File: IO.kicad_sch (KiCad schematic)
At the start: 19 parts, among them J502 I2C, J503 SPI, J601 JST_SHBM04B-SRSS-TB, SW601 B3U-3000P, SW602 B3U-3000P, U601 SHTC3, U602 74LVC1G07SE-7, U603 74LVC1G07SE-7

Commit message: power symbols
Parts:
- removed U603: 74LVC1G07SE-7, Package_TO_SOT_SMD:SOT-353_SC-70-5, symbol CM4IO:74LVC1G07_copy
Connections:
- net nLED_ACTIVITY: now reaches R606.2
- net 3V3 renamed +3V3_PI
- net +3V3_PI: now also D606.2 (A)
- net 5V renamed +5V
- net +5V: no longer D606.2 (A)

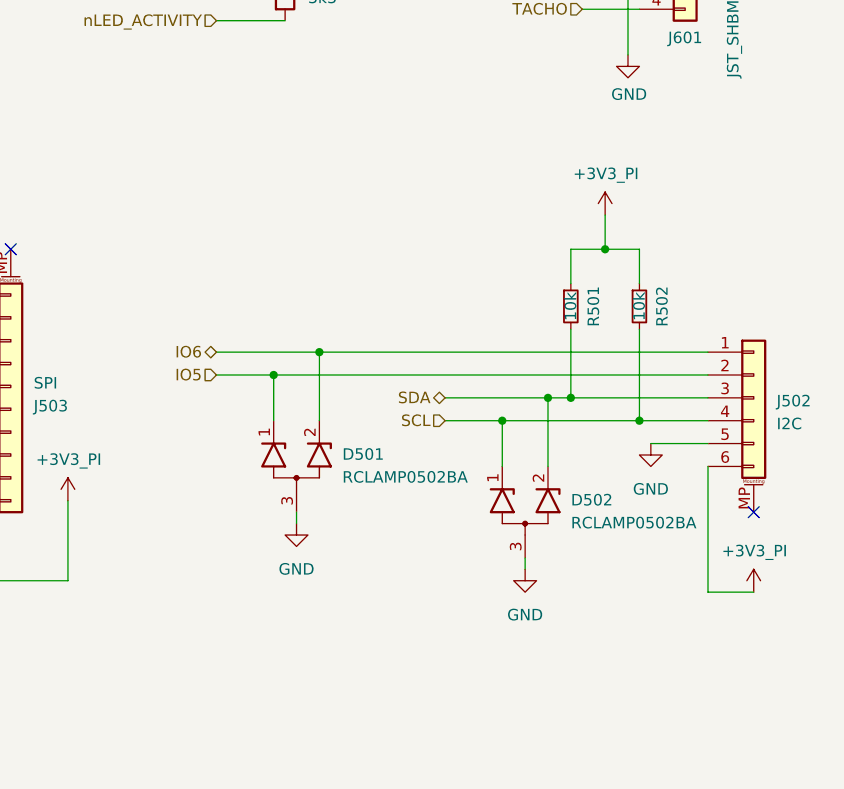
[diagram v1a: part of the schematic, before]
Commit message: changed i2c connector and nrpiboot
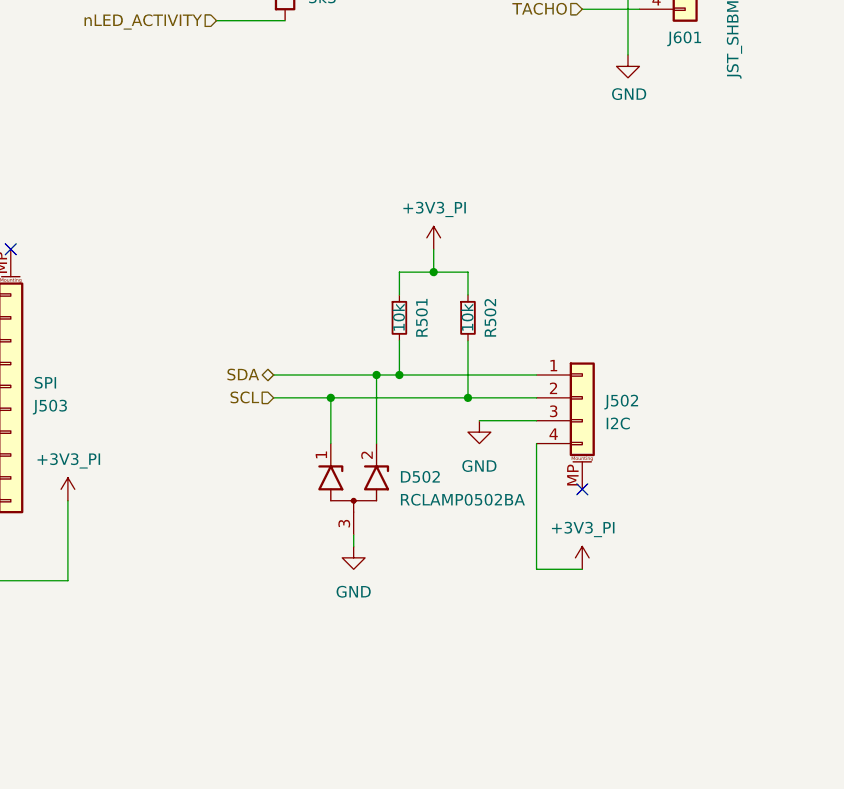
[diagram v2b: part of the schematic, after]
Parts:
- removed D501: RCLAMP0502BA, Package_TO_SOT_SMD:SOT-416, symbol Power_Protection:RCLAMP0502BA
- J502: footprint Connector_JST:JST_SH_BM06B-SRSS-TB_1x06-1MP_P1.00mm_Vertical -> Connector_JST:JST_SH_BM04B-SRSS-TB_1x04-1MP_P1.00mm_Vertical; symbol Connector_Generic_MountingPin:Conn_01x06_MountingPin -> Connector_Generic_MountingPin:Conn_01x04_MountingPin
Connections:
- net IO5 is gone; now on net SCL: J502.2 (Pin_2)
- net IO6 is gone; now on net SDA: J502.1 (Pin_1)
- net +3V3_PI: now also J502.4 (Pin_4); no longer J502.6 (Pin_6)
- net GND: now also J502.3 (Pin_3); no longer J502.5 (Pin_5)
- net SCL: no longer J502.4 (Pin_4)
- net SDA: no longer J502.3 (Pin_3)
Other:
- moved on the sheet: D502, R501, R502

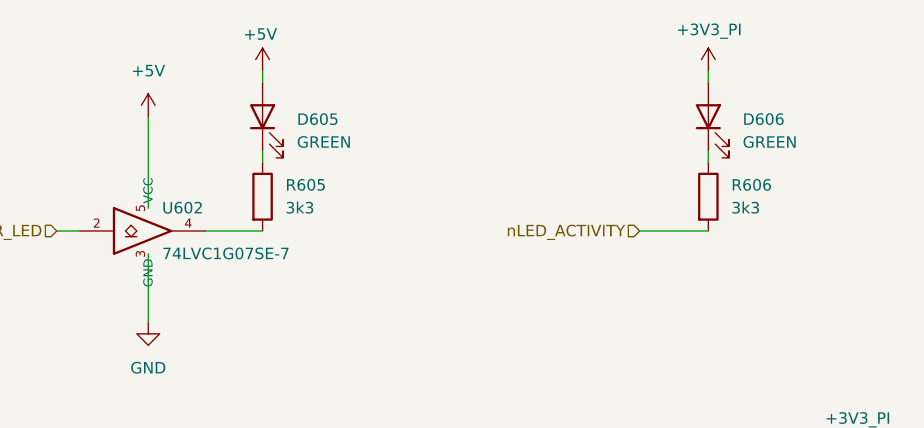
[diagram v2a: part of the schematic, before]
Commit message: esd HDMI complete
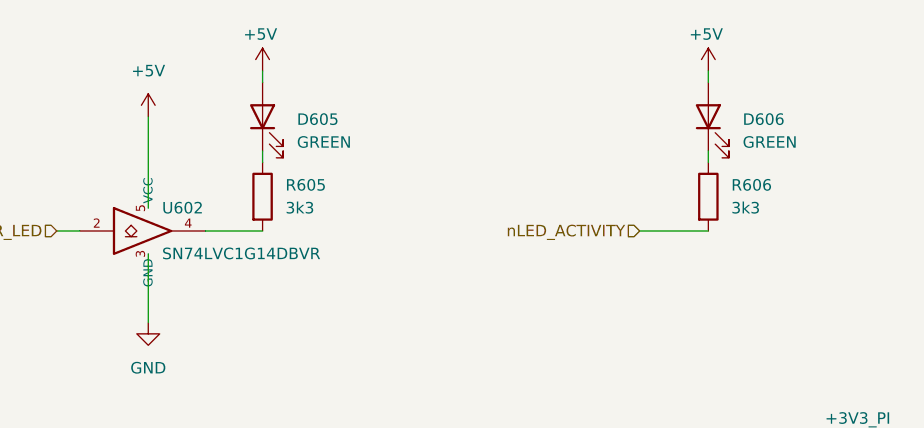
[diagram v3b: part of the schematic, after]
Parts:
- U602: value 74LVC1G07SE-7 -> SN74LVC1G14DBVR; P/N 74LVC1G07SE-7 -> SN74LVC1G14DBVR
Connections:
- net +3V3_PI: no longer D606.2 (A)
- net +5V: now also D606.2 (A)
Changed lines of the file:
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@@
+	(symbol
+		(lib_id "power:+5V")
+		(at 138.43 17.78 0)
+		(unit 1)
+		(exclude_from_sim no)
+		(in_bom yes)
+		(on_board yes)
+		(dnp no)
+		(property "Reference" "#PWR0510"
+			(at 138.43 21.59 0)
+			(effects
+				(font
+					(size 1.27 1.27)
+				)
+				(hide yes)
+			)
+		)
+		(property "Value" "+5V"
+			(at 138.176 13.716 0)
+			(effects
+				(font
+					(size 1.27 1.27)
+				)
+			)
+		)
+		(property "Footprint" ""
+			(at 138.43 17.78 0)
+			(effects
+				(font
+					(size 1.27 1.27)
+				)
+				(hide yes)
+			)
+		)
+		(property "Datasheet" ""
+			(at 138.43 17.78 0)
+			(effects
+				(font
+					(size 1.27 1.27)
+				)
+				(hide yes)
+			)
+		)
+		(property "Description" "Power symbol creates a global label with name \"+5V\""
+			(at 138.43 17.78 0)
+			(effects
+				(font
+					(size 1.27 1.27)
+				)
+				(hide yes)
+			)
+		)
+		(pin "1"
+		)
+		(instances
+			(project "CM5_MINIMA_2"
+				(path "/b33e81d6-18a9-4b9d-a239-76a7c253462f/4ce4cfa7-ba20-49b9-8014-333351d4c7f7"
+					(reference "#PWR0510")
+					(unit 1)
+				)
+			)
+		)
+	)
 	(symbol
 		(lib_id "power:+5V")
@@
 			)
 		)
-		(property "Value" "74LVC1G07SE-7"
+		(property "Value" "SN74LVC1G14DBVR"
 			(at 77.724 38.1 0)
 			(effects
@@
 			)
 		)
-		(property "Datasheet" "https://www.diodes.com/assets/Datasheets/74LVC1G07.pdf"
+		(property "Datasheet" "https://www.lcsc.com/datasheet/lcsc_datasheet_2405141143_UMW-Youtai-Semiconductor-Co---Ltd--SN74LVC1G14DBVR_C434069.pdf"
 			(at 76.2 35.56 0)
 			(effects
@@
 			)
 		)
-		(property "P/N" "74LVC1G07SE-7"
+		(property "P/N" "SN74LVC1G14DBVR"
 			(at 76.2 35.56 0)
 			(effects
@@
 					(unit 1)
 				)
-			)
-		)
-	)
-	(symbol
-		(lib_id "power:+3V3")
-		(at 138.43 17.78 0)
-		(unit 1)
-		(exclude_from_sim no)
-		(in_bom yes)
-		(on_board yes)
-		(dnp no)
-		(property "Reference" "#PWR0518"
-			(at 138.43 21.59 0)
-			(effects
-				(font
-					(size 1.27 1.27)
-				)
-				(hide yes)
-			)
-		)
-		(property "Value" "+3V3_PI"
-			(at 134.874 13.208 0)
-			(effects
-				(font
-					(size 1.27 1.27)
-				)
-				(justify left)
-			)
-		)
-		(property "Footprint" ""
-			(at 138.43 17.78 0)
-			(effects
-				(font
-					(size 1.27 1.27)
-				)
-				(hide yes)
-			)
-		)
-		(property "Datasheet" ""
-			(at 138.43 17.78 0)
-			(effects
-				(font
-					(size 1.27 1.27)
-				)
-				(hide yes)
-			)
-		)
-		(property "Description" "Power symbol creates a global label with name \"+3V3\""
-			(at 138.43 17.78 0)
-			(effects
-				(font
-					(size 1.27 1.27)
-				)
-				(hide yes)
-			)
-		)
-		(pin "1"
-		)
-		(instances
-			(project "CM5_MINIMA_2"
-				(path "/b33e81d6-18a9-4b9d-a239-76a7c253462f/4ce4cfa7-ba20-49b9-8014-333351d4c7f7"
-					(reference "#PWR0518")
-					(unit 1)
-				)
